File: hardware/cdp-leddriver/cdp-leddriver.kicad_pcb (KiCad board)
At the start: 2 copper layers, 99.1 x 99.1 mm, 42 parts, among them J1 Conn_02x20_Odd_Even, J2 Conn_02x20_Odd_Even, J3 Conn_01x09_Pin, J4 Conn_01x09_Pin, J5 Conn_01x09_Pin, J6 Conn_01x09_Pin, J7 Conn_01x05_Pin, J8 Conn_01x06_Pin, U1 74LS574, U2 74LS573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

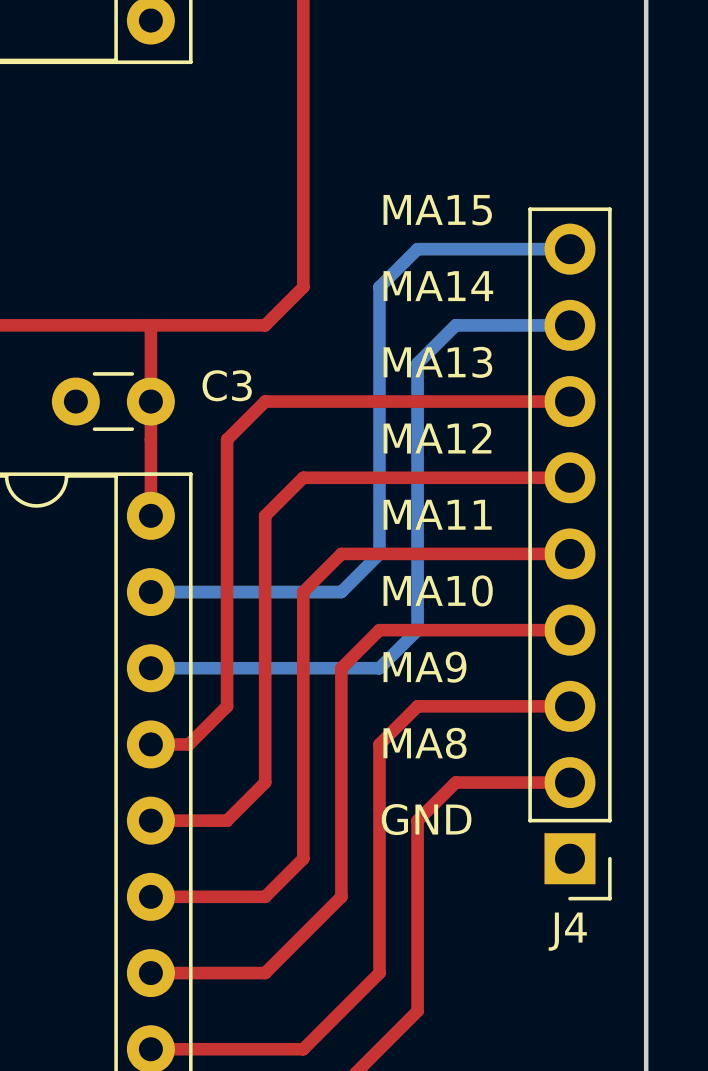
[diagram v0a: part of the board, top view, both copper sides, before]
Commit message: IC names fixed on the led driver schematic, on the PCB the MA8-MA15 labels were misaligned that is also fixed. Updated the gerber files.
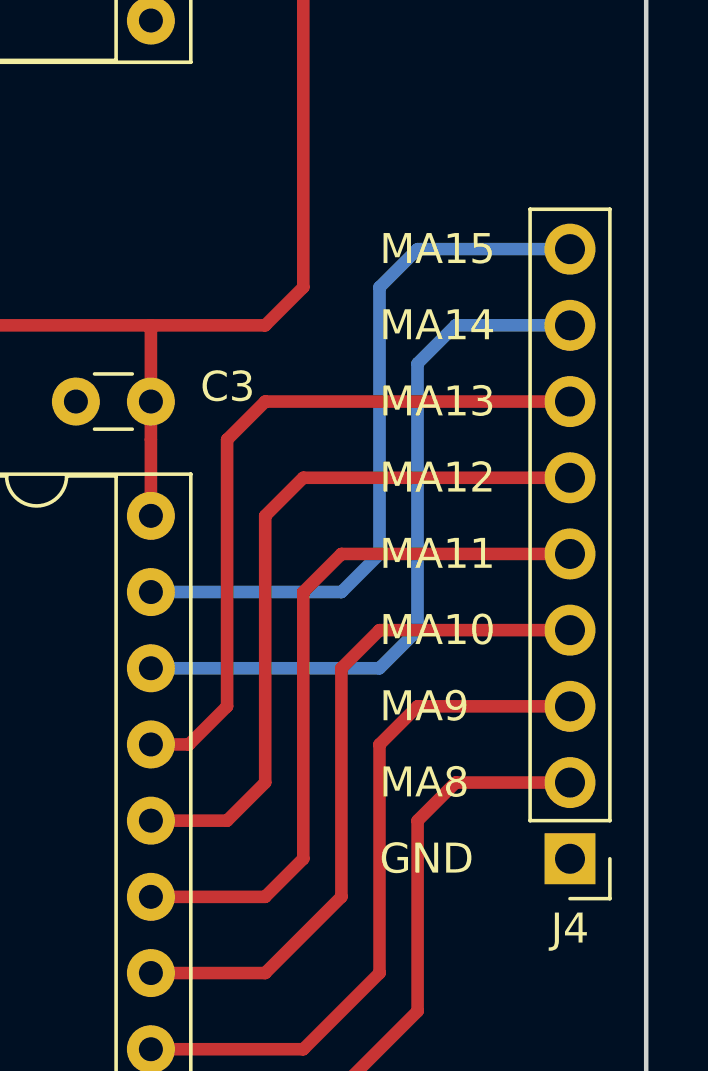
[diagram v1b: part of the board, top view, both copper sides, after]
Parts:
- U1, U3, U4: value 74LS574 -> 74HC574
- U2: value 74LS573 -> 74HC573
- U5, U7, U9: value 74LS74 -> 74HC74
- U6, U8: value 74LS132 -> 74HC132
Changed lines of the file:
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@@
         (effects (font (size 1 1) (thickness 0.15)))
     )
-    (fp_text value "74LS74" (at 3.81 17.57) (layer "F.Fab")
+    (fp_text value "74HC74" (at 3.81 17.57) (layer "F.Fab")
         (effects (font (size 1 1) (thickness 0.15)))
     )
@@
         (effects (font (size 1 1) (thickness 0.15)))
     )
-    (fp_text value "74LS574" (at 3.81 25.19) (layer "F.Fab")
+    (fp_text value "74HC574" (at 3.81 25.19) (layer "F.Fab")
         (effects (font (size 1 1) (thickness 0.15)))
     )
@@
         (effects (font (size 1 1) (thickness 0.15)))
     )
-    (fp_text value "74LS74" (at 3.81 17.57) (layer "F.Fab")
+    (fp_text value "74HC74" (at 3.81 17.57) (layer "F.Fab")
         (effects (font (size 1 1) (thickness 0.15)))
     )
@@
         (effects (font (size 1 1) (thickness 0.15)))
     )
-    (fp_text value "74LS574" (at 3.81 25.19) (layer "F.Fab")
+    (fp_text value "74HC574" (at 3.81 25.19) (layer "F.Fab")
         (effects (font (size 1 1) (thickness 0.15)))
     )
@@
         (effects (font (size 1 1) (thickness 0.15)))
     )
-    (fp_text value "74LS132" (at 3.81 17.57) (layer "F.Fab")
+    (fp_text value "74HC132" (at 3.81 17.57) (layer "F.Fab")
         (effects (font (size 1 1) (thickness 0.15)))
     )
@@
         (effects (font (size 1 1) (thickness 0.15)))
     )
-    (fp_text value "74LS74" (at 3.81 17.57) (layer "F.Fab")
+    (fp_text value "74HC74" (at 3.81 17.57) (layer "F.Fab")
         (effects (font (size 1 1) (thickness 0.15)))
     )
@@
         (effects (font (size 1 1) (thickness 0.15)))
     )
-    (fp_text value "74LS573" (at 3.81 25.19) (layer "F.Fab")
+    (fp_text value "74HC573" (at 3.81 25.19) (layer "F.Fab")
         (effects (font (size 1 1) (thickness 0.15)))
     )
@@
         (effects (font (size 1 1) (thickness 0.15)))
     )
-    (fp_text value "74LS132" (at 3.81 17.57) (layer "F.Fab")
+    (fp_text value "74HC132" (at 3.81 17.57) (layer "F.Fab")
         (effects (font (size 1 1) (thickness 0.15)))
     )
@@
         (effects (font (size 1 1) (thickness 0.15)))
     )
-    (fp_text value "74LS574" (at 3.81 25.19) (layer "F.Fab")
+    (fp_text value "74HC574" (at 3.81 25.19) (layer "F.Fab")
         (effects (font (size 1 1) (thickness 0.15)))
     )
@@
     (effects (font (size 1 1) (thickness 0.15)) (justify left))
   )
-  (gr_text "MA12" (at 198.12 115.57) (layer "F.SilkS")
+  (gr_text "MA12" (at 198.12 116.84) (layer "F.SilkS")
     (effects (font (size 1 1) (thickness 0.15)) (justify left))
   )
@@
     (effects (font (size 1 1) (thickness 0.15)) (justify left))
   )
-  (gr_text "MA8" (at 198.12 125.73) (layer "F.SilkS")
+  (gr_text "MA8" (at 198.12 127) (layer "F.SilkS")
     (effects (font (size 1 1) (thickness 0.15)) (justify left))
   )
@@
     (effects (font (size 1 1) (thickness 0.15)) (justify left))
   )
-  (gr_text "MA9" (at 198.12 123.19) (layer "F.SilkS")
+  (gr_text "MA9" (at 198.12 124.46) (layer "F.SilkS")
     (effects (font (size 1 1) (thickness 0.15)) (justify left))
   )
@@
     (effects (font (size 1 1) (thickness 0.15)) (justify left))
   )
-  (gr_text "MA11" (at 198.12 118.11) (layer "F.SilkS")
+  (gr_text "MA11" (at 198.12 119.38) (layer "F.SilkS")
     (effects (font (size 1 1) (thickness 0.15)) (justify left))
   )
-  (gr_text "MA14" (at 198.12 110.49) (layer "F.SilkS")
+  (gr_text "MA14" (at 198.12 111.76) (layer "F.SilkS")
     (effects (font (size 1 1) (thickness 0.15)) (justify left))
   )
@@
     (effects (font (size 1 1) (thickness 0.15)) (justify left))
   )
-  (gr_text "MA15" (at 198.12 107.95) (layer "F.SilkS")
+  (gr_text "MA15" (at 198.12 109.22) (layer "F.SilkS")
     (effects (font (size 1 1) (thickness 0.15)) (justify left))
   )
@@
     (effects (font (size 1 1) (thickness 0.15)) (justify left))
   )
-  (gr_text "GND" (at 198.12 128.27) (layer "F.SilkS")
+  (gr_text "GND" (at 198.12 129.54) (layer "F.SilkS")
     (effects (font (size 1 1) (thickness 0.15)) (justify left))
   )
@@
     (effects (font (size 1 1) (thickness 0.15)) (justify left))
   )
-  (gr_text "MA13" (at 198.12 113.03) (layer "F.SilkS")
+  (gr_text "MA13" (at 198.12 114.3) (layer "F.SilkS")
     (effects (font (size 1 1) (thickness 0.15)) (justify left))
   )
@@
     (effects (font (size 1 1) (thickness 0.15)) (justify left))
   )
-  (gr_text "MA10" (at 198.12 120.65) (layer "F.SilkS")
+  (gr_text "MA10" (at 198.12 121.92) (layer "F.SilkS")
     (effects (font (size 1 1) (thickness 0.15)) (justify left))
   )
